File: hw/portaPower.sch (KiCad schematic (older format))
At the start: 2 parts

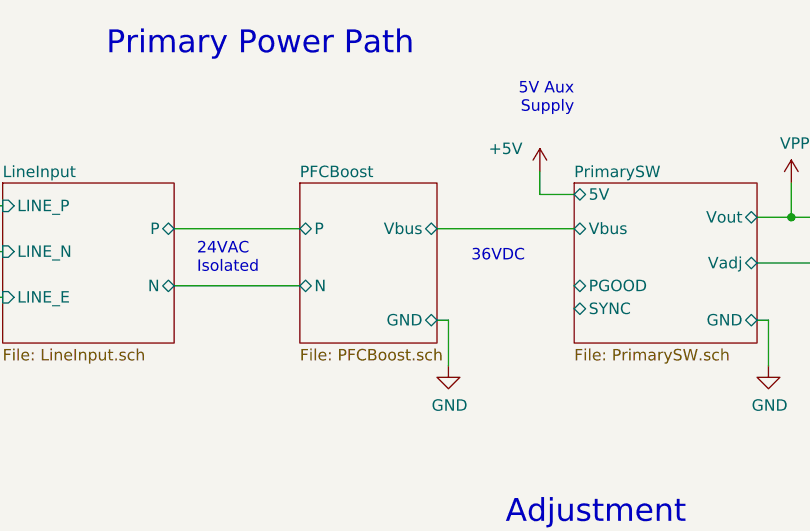
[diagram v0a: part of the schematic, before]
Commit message: More work on PFC
Added more circuitry to PFC boost converter; about half done
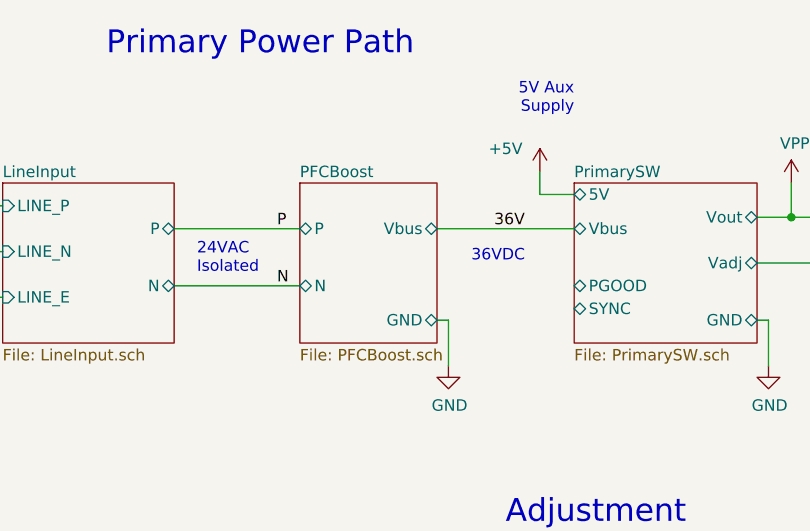
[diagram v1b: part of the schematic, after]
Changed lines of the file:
@@
 Text Notes 4000 2800 0    100  ~ 0
 Adjustment
+Text Label 3950 1500 0    50   ~ 0
+36V
+Text Label 3000 1500 0    50   ~ 0
+P
+Text Label 3000 1750 0    50   ~ 0
+N
 $EndSCHEMATC

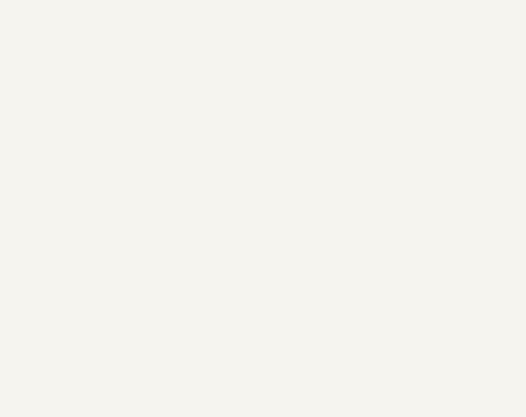
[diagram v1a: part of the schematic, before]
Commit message: Primary SW component selection
selected some components for primary switcher, added AuxOut block, dropped down primary linear reg IC
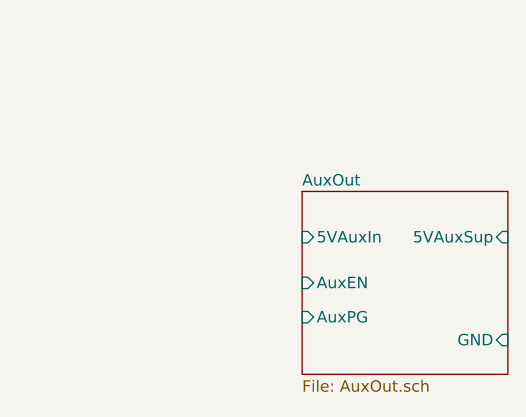
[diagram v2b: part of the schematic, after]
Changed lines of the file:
@@
 $Descr A4 11693 8268
 encoding utf-8
-Sheet 1 6
+Sheet 1 7
 Title ""
 Date ""
@@
 Text Label 3000 1750 0    50   ~ 0
 N
+$Sheet
+S 8000 4150 900  800
+U 5EB6CA11
+F0 "AuxOut" 50
+F1 "AuxOut.sch" 50
+F2 "GND" I R 8900 4800 50
+F3 "5VAuxSup" I R 8900 4350 50
+F4 "5VAuxIn" I L 8000 4350 50
+F5 "AuxEN" I L 8000 4550 50
+F6 "AuxPG" I L 8000 4700 50
+$EndSheet
 $EndSCHEMATC
